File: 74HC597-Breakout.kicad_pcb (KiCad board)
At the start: 2 copper layers, 17 parts, among them J1 Conn_01x07, J2 Conn_01x07, J3 Conn_01x08, J4 Conn_01x07, J5 Conn_01x07, J6 Conn_01x08, U1 74HC597

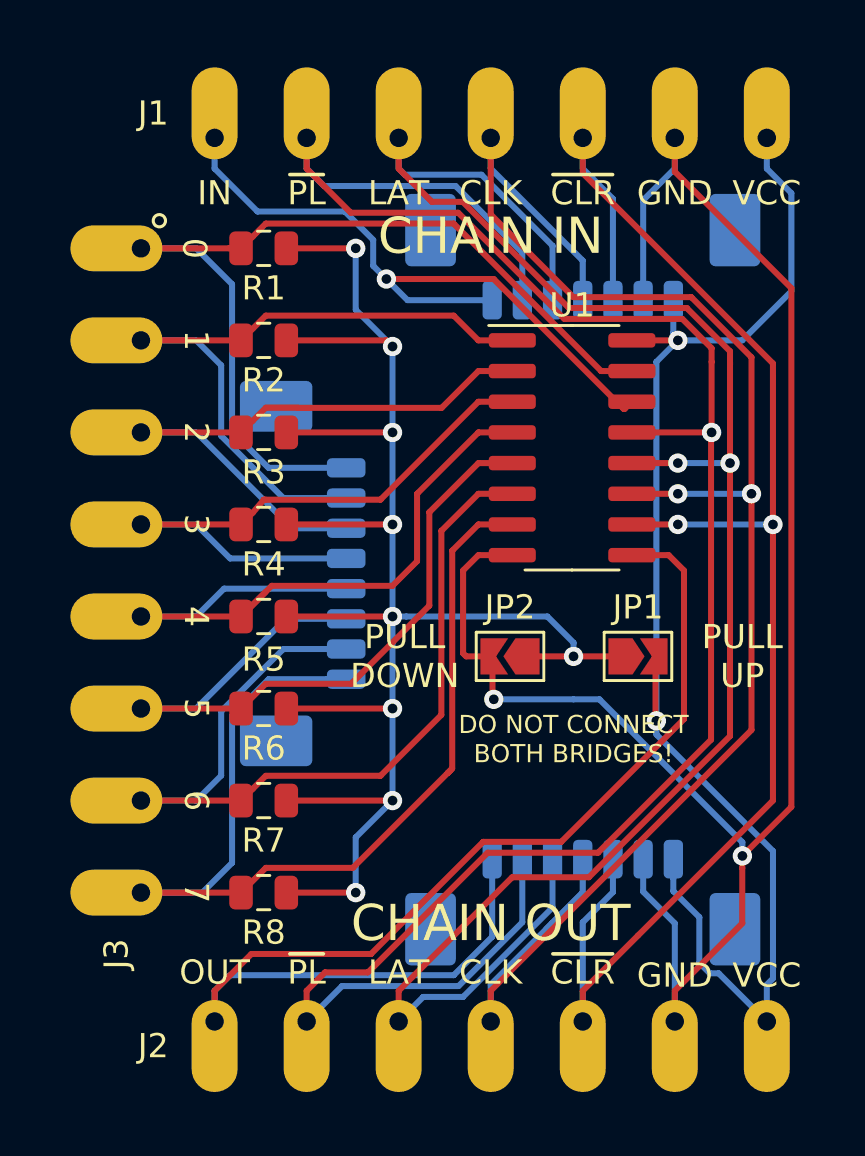
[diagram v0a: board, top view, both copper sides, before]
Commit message: Local symbols into project lib, also plots
Plotted gerbers and schematic
Moved symbol into a local library
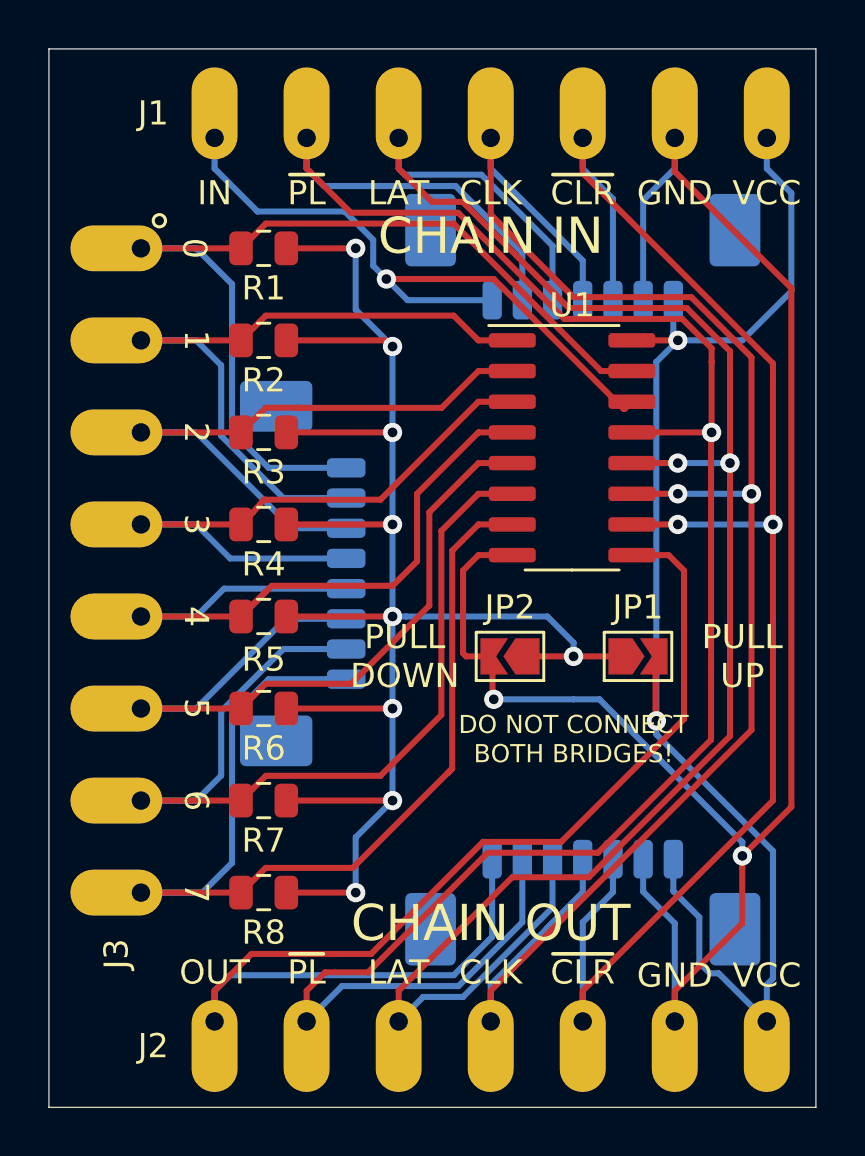
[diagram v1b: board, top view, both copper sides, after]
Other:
- board outline added: 31.7 x 43.8 mm
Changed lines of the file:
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@@
   (general
     (thickness 1.6)
-    (drawings 39)
+    (drawings 43)
     (tracks 307)
     (zones 0)
@@
     (visible_elements FFFFFF7F)
     (pcbplotparams
-      (layerselection 0x010fc_ffffffff)
+      (layerselection 0x010f0_ffffffff)
       (usegerberextensions false)
       (usegerberattributes false)
@@
       (outputformat 1)
       (mirror false)
-      (drillshape 1)
+      (drillshape 0)
       (scaleselection 1)
-      (outputdirectory ""))
+      (outputdirectory "gerbers/"))
   )
   (net 0 "")
@@
     )
   )
+  (gr_line (start 157.48 137.16) (end 157.48 93.345) (layer Edge.Cuts) (width 0.05))
+  (gr_line (start 125.73 137.16) (end 157.48 137.16) (layer Edge.Cuts) (width 0.05))
+  (gr_line (start 125.73 93.345) (end 125.73 137.16) (layer Edge.Cuts) (width 0.05))
+  (gr_line (start 157.48 93.345) (end 125.73 93.345) (layer Edge.Cuts) (width 0.05))
   (gr_text ~PL (at 136.398 99.314) (layer F.SilkS)
     (effects (font (size 1 1) (thickness 0.15)))
